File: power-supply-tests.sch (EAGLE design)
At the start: 14 parts, among them U2 POWER-VREG-EN-SW-500MA

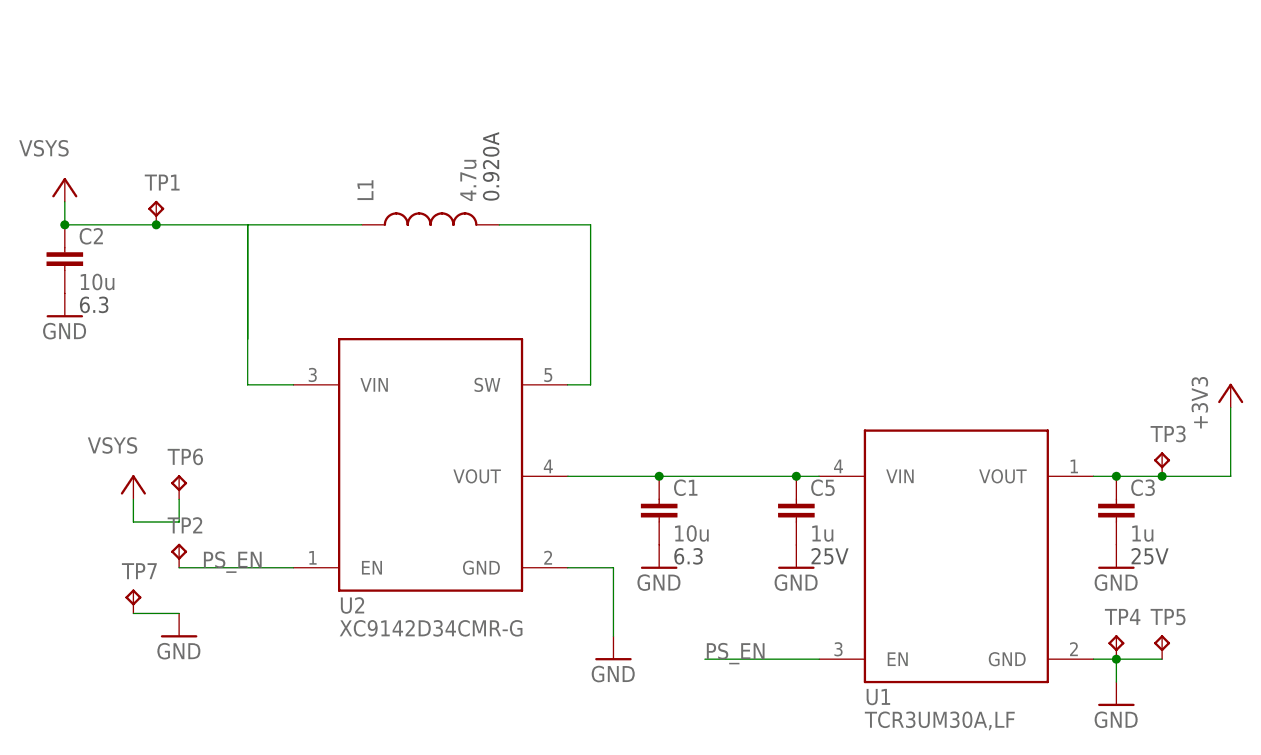
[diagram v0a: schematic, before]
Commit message: Latest changes to nRF91
Changed:
* Power supply inductor
* Power supply tests board updated
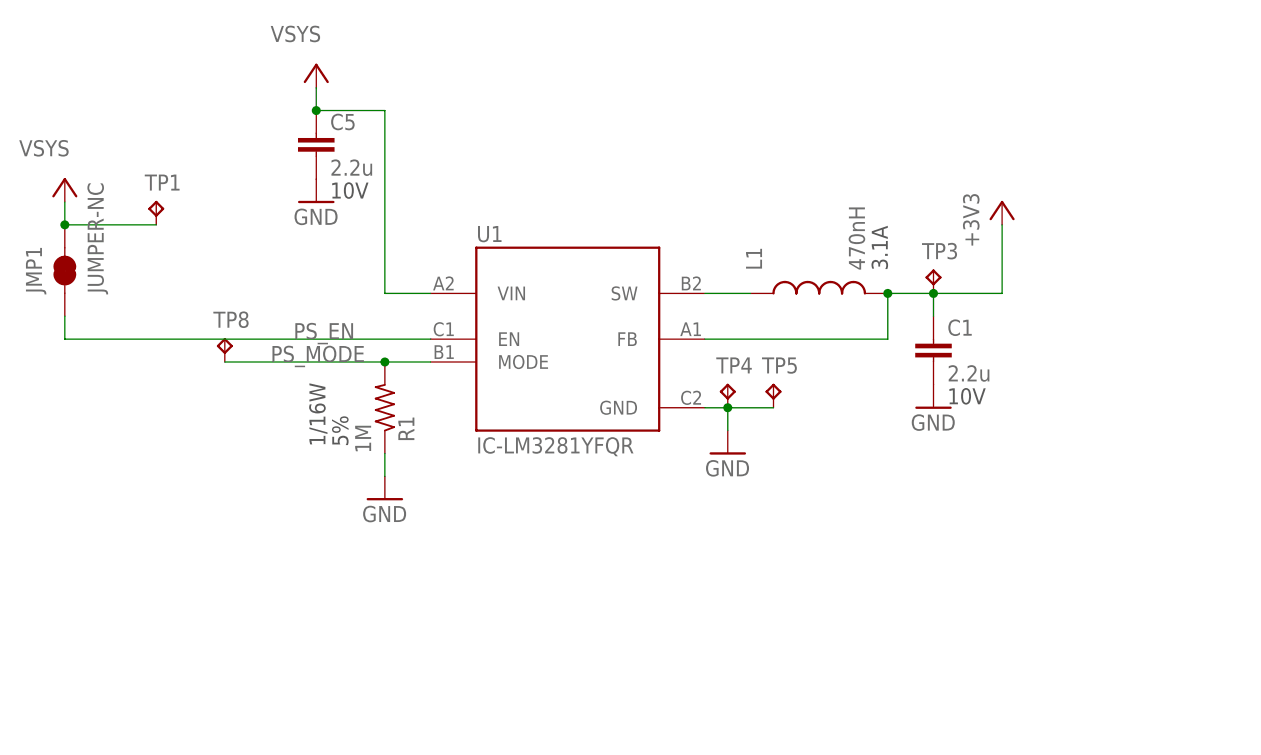
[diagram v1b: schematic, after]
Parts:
- removed C2: 10u, wolff-den:CAP-10U-6.3V-0603
- removed C3: 1u, wolff-den:CAP-1U-25V-1-0402
- removed TP2, TP6, TP7: HEADER-1, wolff-den:HEADER-1
- removed U2: POWER-VREG-EN-SW-500MA, wolff-den:POWER-VREG-EN-SW-500MA
- added JMP1: JUMPER-NC, wolff-den:JUMPER-NC
- added R1: 1M, wolff-den:RES-1M-5%-0402
- added TP8: HEADER-1, wolff-den:HEADER-1
- C1: value 10u -> 2.2u; device wolff-den:CAP-10U-6.3V-0603 -> wolff-den:CAP-2.2U-10V-01-0603
- C5: value 1u -> 2.2u; device wolff-den:CAP-1U-25V-1-0402 -> wolff-den:CAP-2.2U-10V-01-0603
- L1: value 4.7u -> 470nH; device wolff-den:IND-4.7U-920MA-2X2 -> wolff-den:IND-3.1A-60MOHM-0805
- U1: value (none) -> IC-LM3281YFQR; device wolff-den:POWER-VREG-EN-3.0V-DFN4-1X1 -> wolff-den:IC-LM3281YFQR
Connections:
- removed net N$1: L1.2, U2.SW
- removed net N$3: C1.1, C5.1, U1.VIN, U2.VOUT
- new net PS_MODE: R1.2, TP8.TP, U1.MODE
- new net PS_SW1: L1.1, U1.SW
- net +3V3: now also C1.1, L1.2, U1.FB; no longer C3.1, U1.VOUT
- net GND: now also R1.1; no longer C2.2, C3.2, TP7.TP, U2.GND
- net PS_EN: now also JMP1.1; no longer TP2.TP, U2.EN
- net VSYS: now also C5.1, JMP1.2, U1.VIN; no longer C2.1, L1.1, TP6.TP, U2.VIN
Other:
- moved on the sheet: C1, C5, L1, TP3, TP4, TP5
